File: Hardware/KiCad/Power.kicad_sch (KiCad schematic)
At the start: 44 parts, among them Q1 NMOS_SO-8, U2 BTN9960LV, U3 BTN9960LV, U4 INA180A2, U6 TSR 0.5-2433

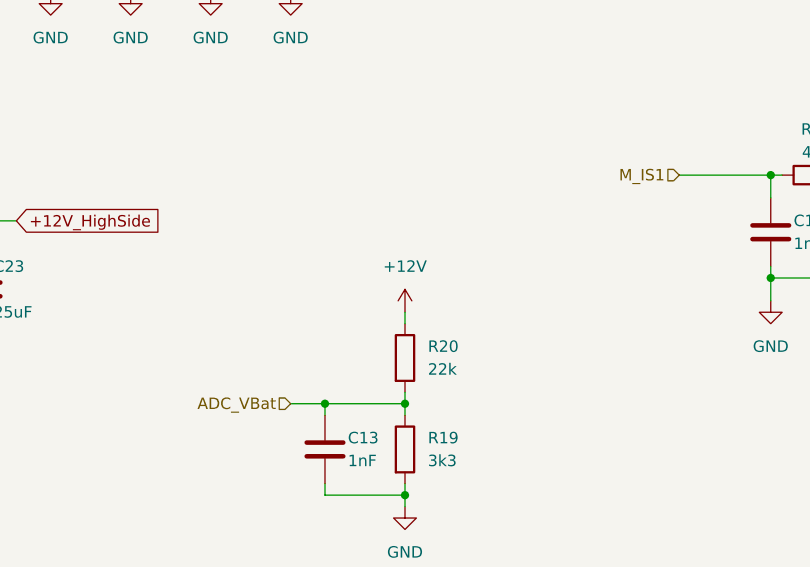
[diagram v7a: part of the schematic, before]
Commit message: update PCB
Add voltage selector solder jumper vor rj45 connector to switch between 12V and 3.3V vor the control panel
Add voltage supression diodes for IS pins from the motor driver ICs
Fix DRC violations
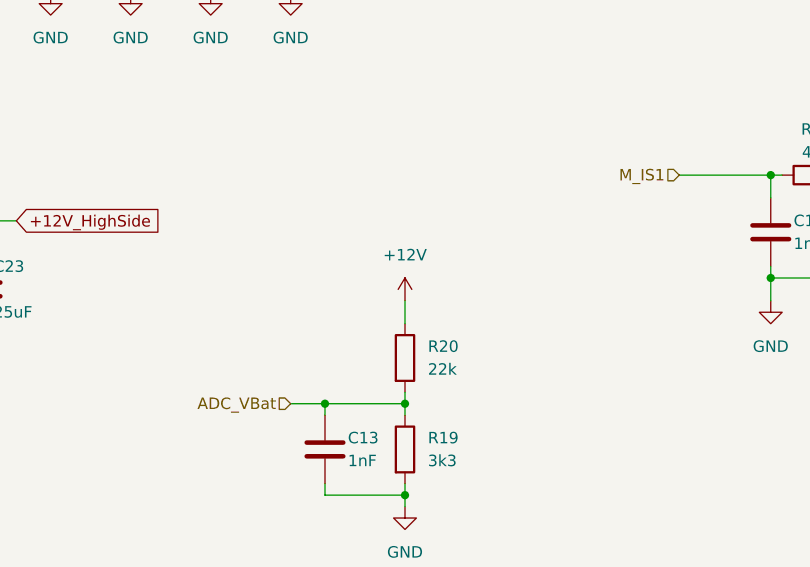
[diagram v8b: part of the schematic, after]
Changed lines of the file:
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@@
     (stroke (width 0) (type default))
   )
-  (wire (pts (xy 129.54 74.93) (xy 129.54 76.2))
+  (wire (pts (xy 129.54 73.66) (xy 129.54 76.2))
     (stroke (width 0) (type default))
   )
@@
     )
   )
-  (symbol (lib_id "power:+12V") (at 129.54 74.93 0) (unit 1)
-    (in_bom yes) (on_board yes) (dnp no) (fields_autoplaced)
-    (property "Reference" "#PWR020" (at 129.54 78.74 0)
-      (effects (font (size 1.27 1.27)) hide)
-    )
-    (property "Value" "+12V" (at 129.54 69.85 0)
-      (effects (font (size 1.27 1.27)))
-    )
-    (property "Footprint" "" (at 129.54 74.93 0)
-      (effects (font (size 1.27 1.27)) hide)
-    )
-    (property "Datasheet" "" (at 129.54 74.93 0)
-      (effects (font (size 1.27 1.27)) hide)
-    )
+  (symbol (lib_id "power:+12V") (at 129.54 73.66 0) (unit 1)
+    (in_bom yes) (on_board yes) (dnp no) (fields_autoplaced)
+    (property "Reference" "#PWR020" (at 129.54 77.47 0)
+      (effects (font (size 1.27 1.27)) hide)
+    )
+    (property "Value" "+12V" (at 129.54 68.58 0)
+      (effects (font (size 1.27 1.27)))
+    )
+    (property "Footprint" "" (at 129.54 73.66 0)
+      (effects (font (size 1.27 1.27)) hide)
+    )
+    (property "Datasheet" "" (at 129.54 73.66 0)
+      (effects (font (size 1.27 1.27)) hide)
+    )
